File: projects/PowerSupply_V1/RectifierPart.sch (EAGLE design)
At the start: 17 parts, among them X1 IN, X2 PRI, X3 SEC, X4 OUT

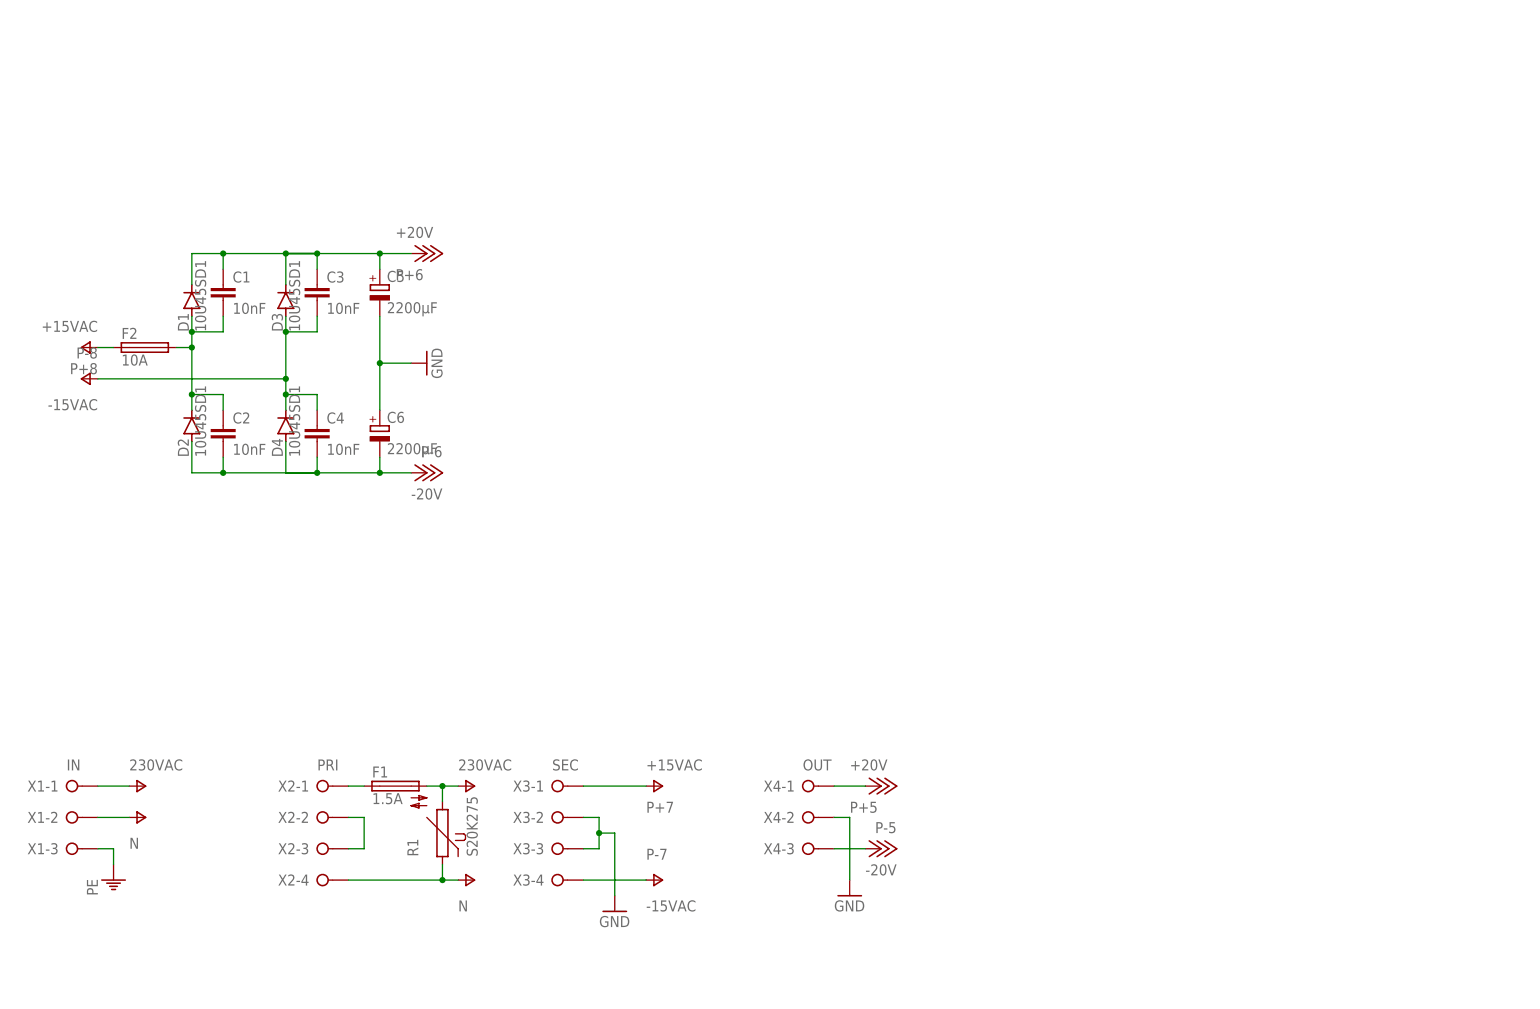
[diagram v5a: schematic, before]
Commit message: feat: rectifier part modified
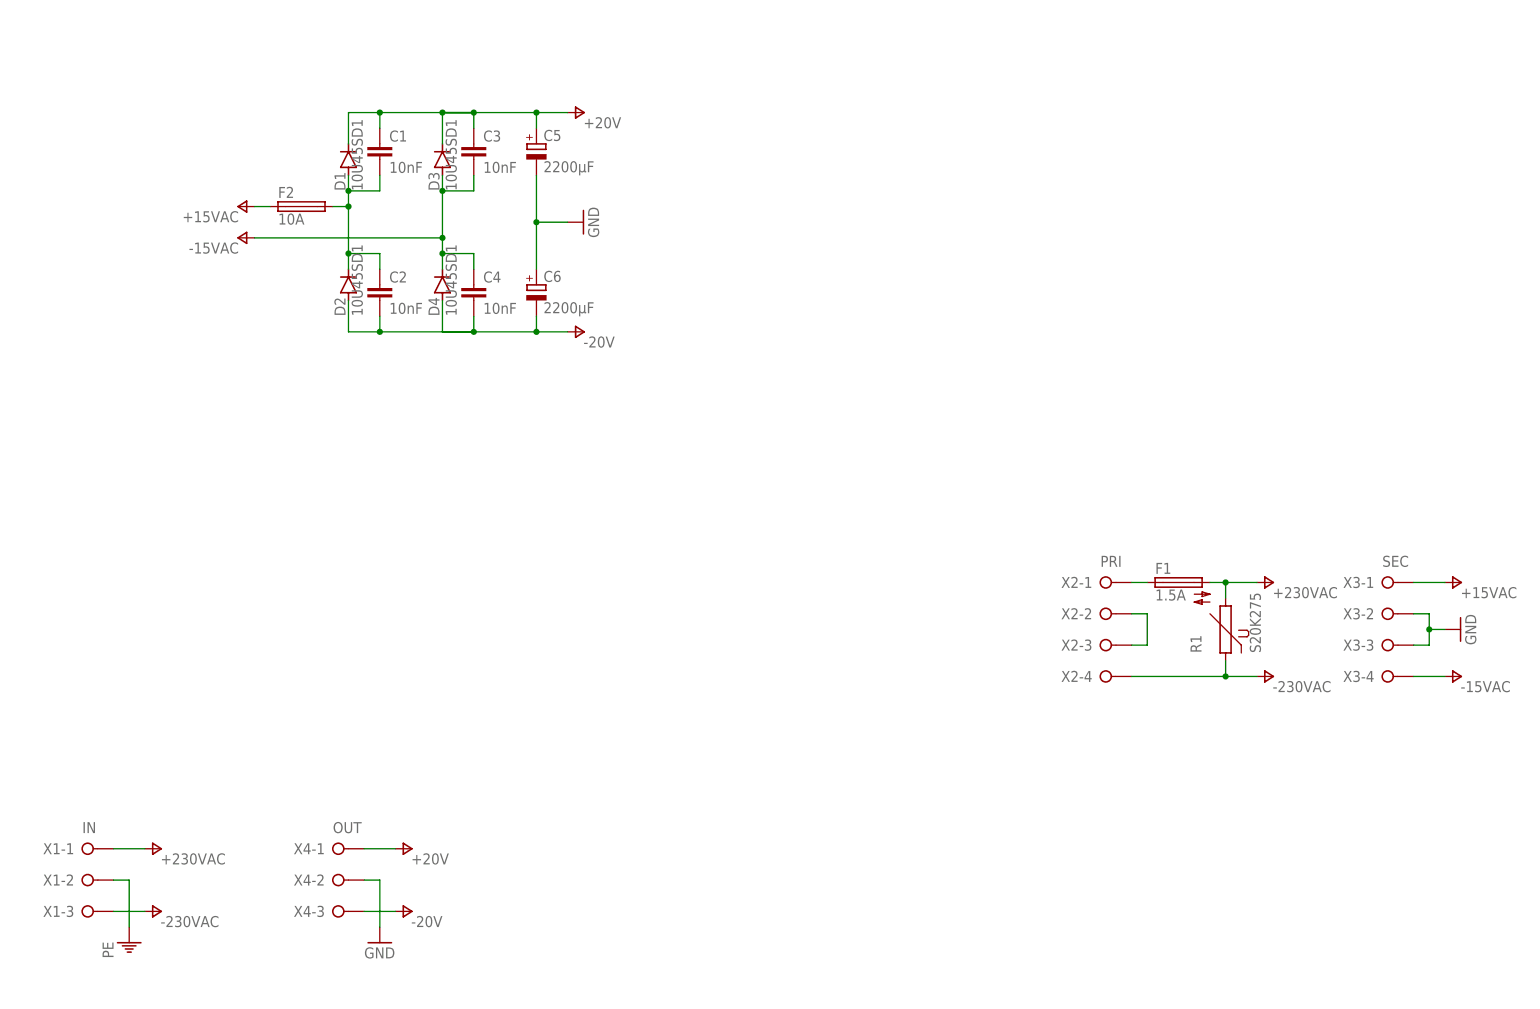
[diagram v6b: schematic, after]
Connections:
- net V+ renamed +230VAC
- removed net V-: R1.1, X1-2.KL, X2-4.KL
- new net -230VAC: R1.1, X1-3.KL, X2-4.KL
- net PE: now also X1-2.KL; no longer X1-3.KL
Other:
- moved on the sheet: C1, C2, C3, C4, C5, C6, D1, D2, D3, D4, F1, F2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

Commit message: feat: rectifier part refactored
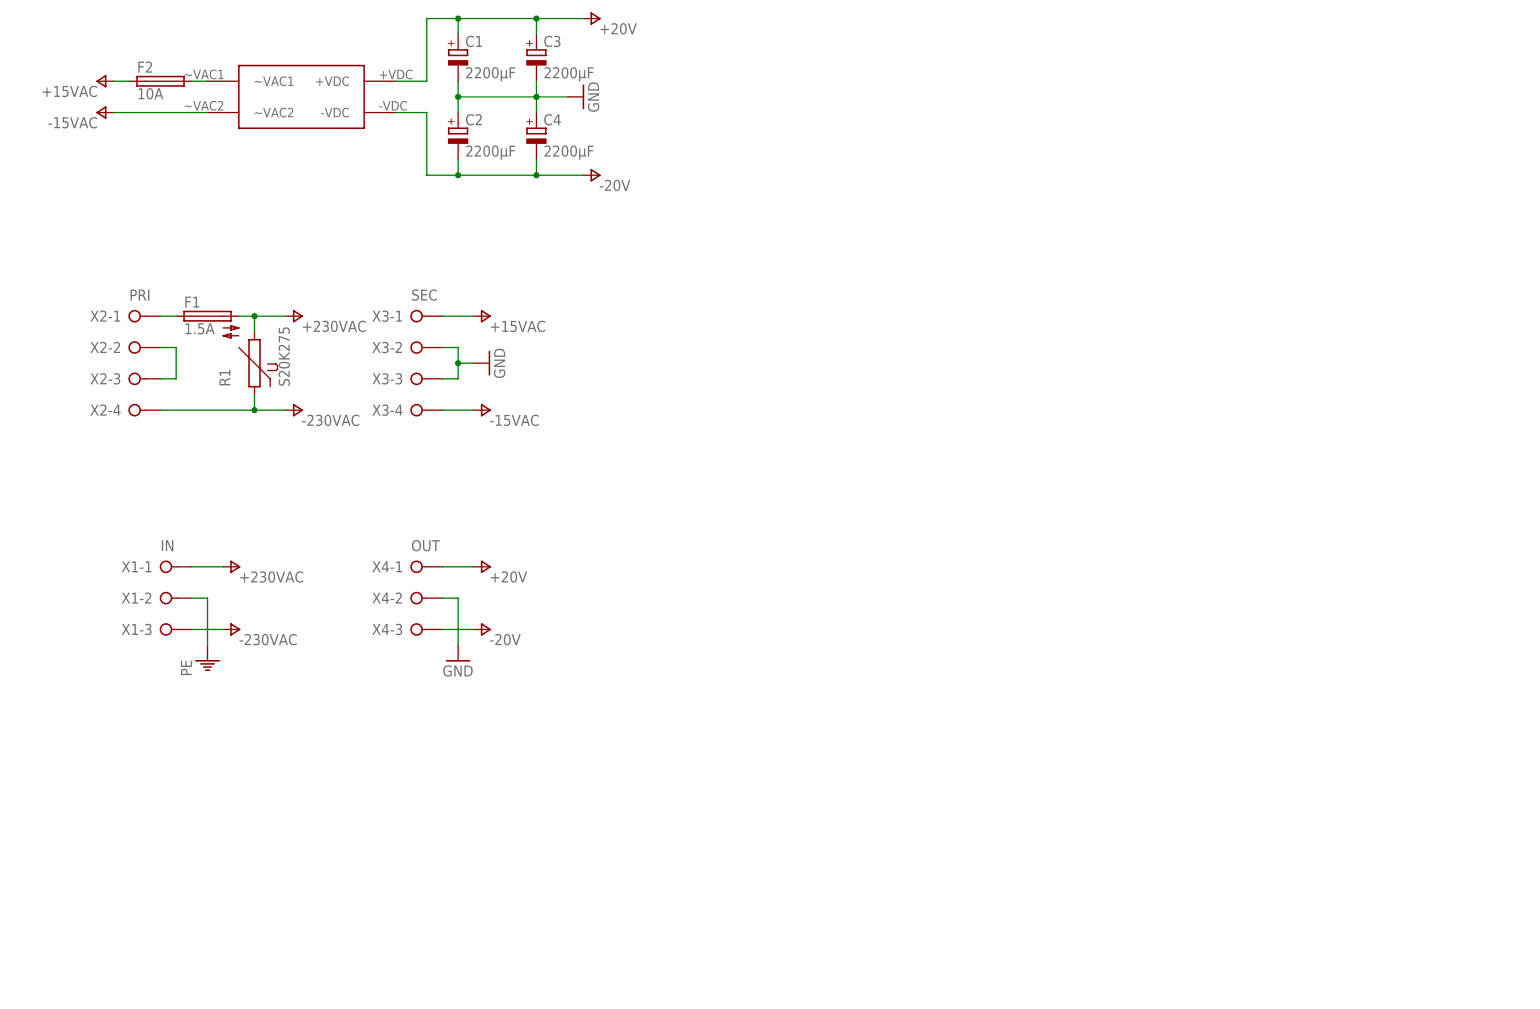
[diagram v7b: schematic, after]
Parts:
- removed C5, C6: 2200µF, rcl:CPOL-EUE7.5-16
- removed D1, D2, D3, D4: 10U45SD1, diode:1N5400
- added R+1: B40C5000-3300A, bb84:B40C5000-3300A
- C1, C2, C3, C4: value 10nF -> 2200µF; device rcl:C-EU050-024X044 -> rcl:CPOL-EUE7.5-16
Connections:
- removed net N$5: C1.2, C2.1, D1.A, D2.C, F2.2
- new net N$1: F2.2, R+1.~VAC1
- net +20V: now also C1.+, C3.+, R+1.+VDC; no longer C1.1, C3.1, C5.+, D1.C, D3.C
- net -15VAC: now also R+1.~VAC2; no longer C3.2, C4.1, D3.A, D4.C
- net -20V: now also C2.-, C4.-, R+1.-VDC; no longer C2.2, C4.2, C6.-, D2.A, D4.A
- net GND: now also C1.-, C2.+, C3.-, C4.+; no longer C5.-, C6.+
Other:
- moved on the sheet: F1, F2, R1, X1-1, X1-2, X1-3, X2-1, X2-2, X2-3, X2-4, X3-1, X3-2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
